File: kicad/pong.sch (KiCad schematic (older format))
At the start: 37 parts, among them J101 power, J102 Y_F, J103 X_F, J104 X, J105 Y, J106 Z, U101 L7805, U102 L7905, U103 TL082, U104 TL082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

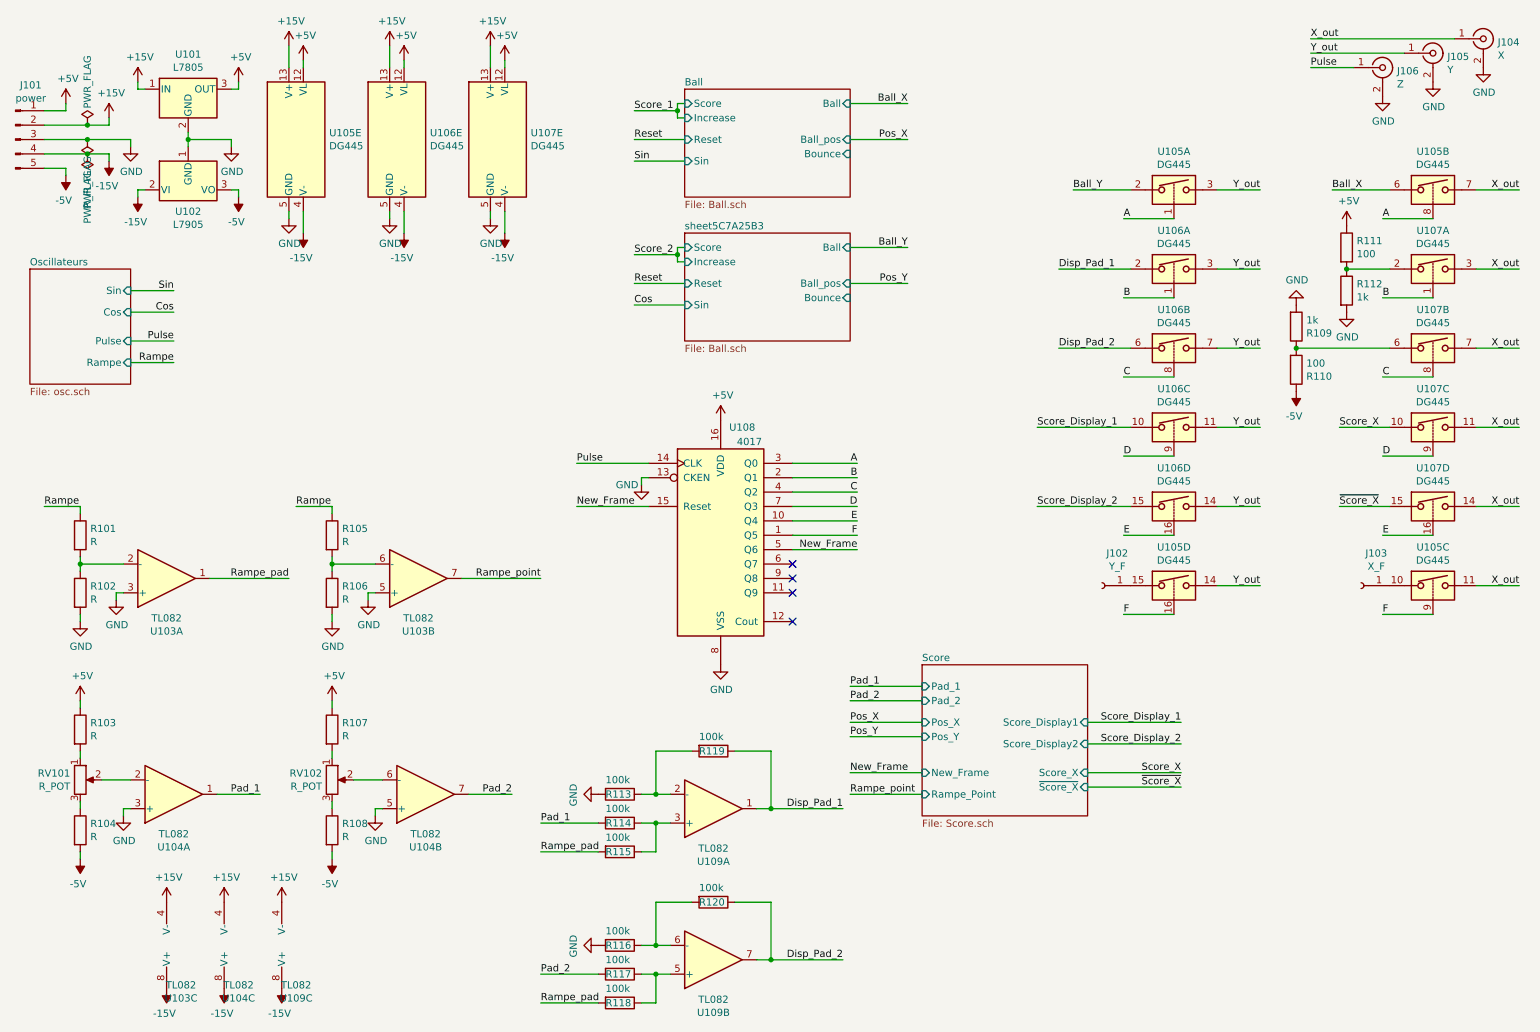
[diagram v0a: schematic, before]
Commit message: Quick fix and documentation
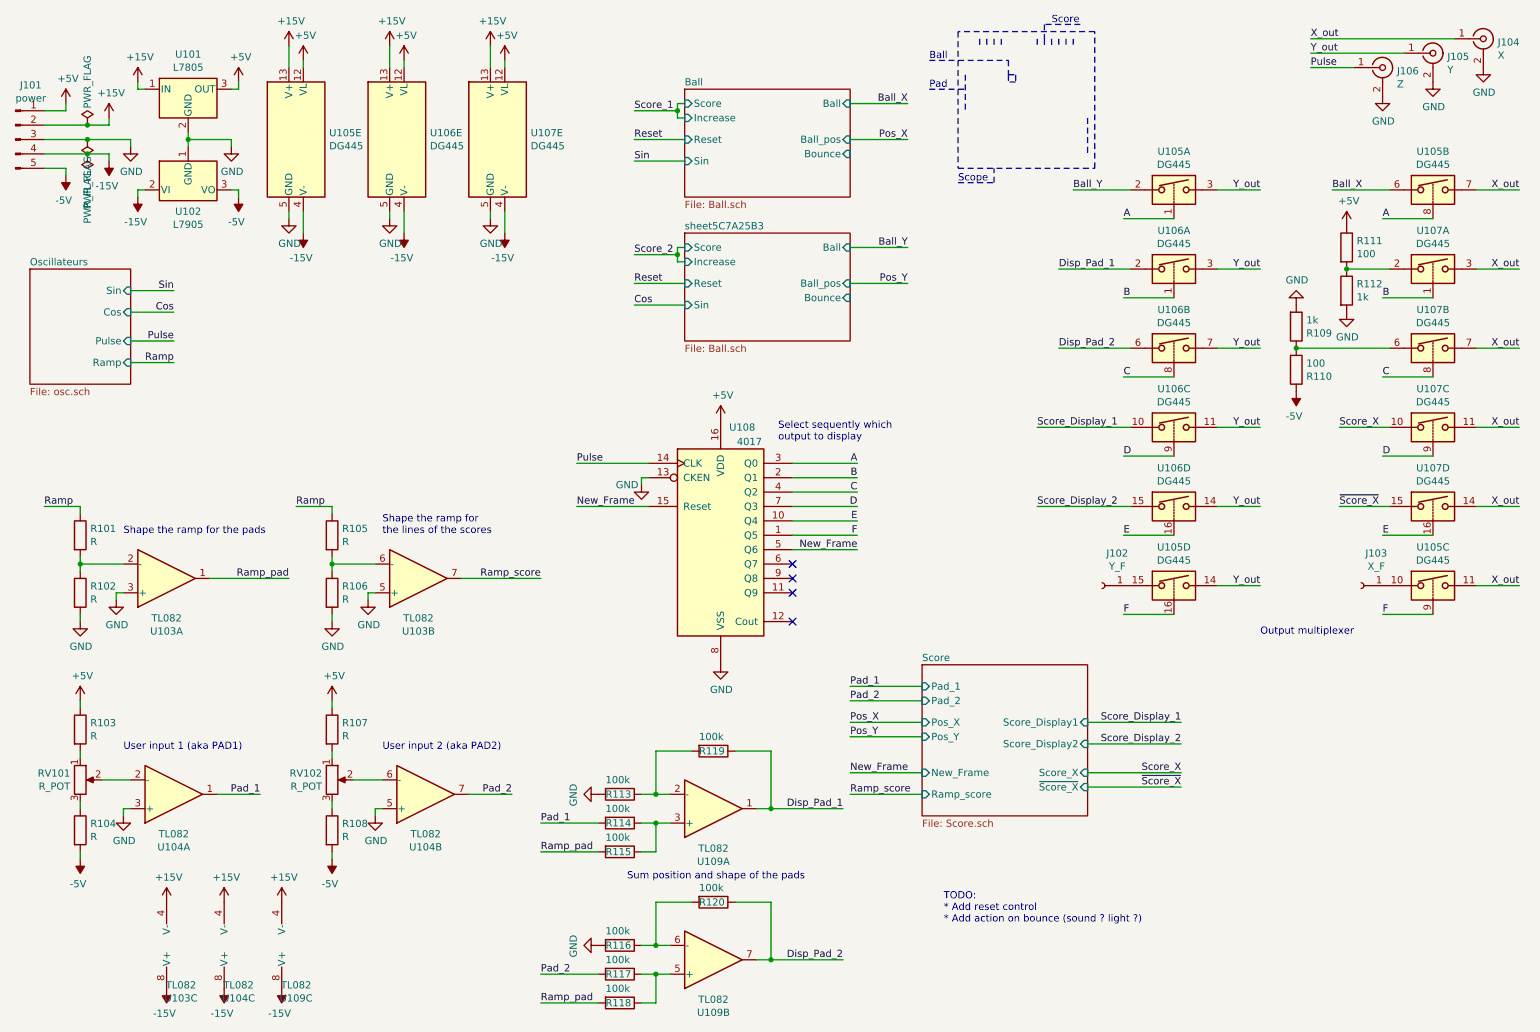
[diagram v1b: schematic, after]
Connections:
- net Rampe renamed Ramp
- net Rampe_pad renamed Ramp_pad
- net Rampe_point renamed Ramp_score
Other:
- note added: "Ball"
- note added: "Output multiplexer"
- note added: "Pad"
- note added: "Scope"
- note added: "Score"
- note added: "Select sequently which\noutput to display"
- note added: "Shape the ramp for \nthe lines of the scores"
- note added: "Shape the ramp for the pads"
- note added: "Sum position and shape of the pads"
- note added: "TODO: \n* Add reset control\n* Add action on bounce (sound ? light ?)"
- note added: "User input 1 (aka PAD1)"
- note added: "User input 2 (aka PAD2)"
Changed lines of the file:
@@
 F2 "Sin" I R 1350 2400 50
 F3 "Cos" I R 1350 2550 50
-F4 "Rampe" I R 1350 2900 50
 F5 "Pulse" I R 1350 2750 50
+F6 "Ramp" I R 1350 2900 50
 $EndSheet
 $Sheet
@@
 F7 "Score_Display2" I R 8000 5550 50
 F8 "Pos_X" I L 6850 5400 50
-F9 "Rampe_Point" I L 6850 5900 50
 F10 "Score_X" I R 8000 5750 50
 F11 "~Score_X" I R 8000 5850 50
+F12 "Ramp_score" I L 6850 5900 50
 $EndSheet
 $Comp
@@
 Pulse
 Text Label 1650 2900 2    50   ~ 0
-Rampe
+Ramp
 Text Label 750  3900 0    50   ~ 0
-Rampe
+Ramp
 Wire Wire Line
 	1900 4400 2450 4400
 Text Label 2450 4400 2    50   ~ 0
-Rampe_pad
+Ramp_pad
 $Comp
 L Device:R R105
@@
 	2750 3900 2500 3900
 Text Label 2500 3900 0    50   ~ 0
-Rampe
+Ramp
 Wire Wire Line
 	3650 4400 4200 4400
 Text Label 4200 4400 2    50   ~ 0
-Rampe_point
+Ramp_score
 $Comp
 L Analog_Switch:DG412xJ U107
@@
 	6350 5900 6850 5900
 Text Label 6350 5900 0    50   ~ 0
-Rampe_point
+Ramp_score
 Wire Wire Line
 	8000 5400 8650 5400
@@
 $EndComp
 Text Label 4200 6300 0    50   ~ 0
-Rampe_pad
+Ramp_pad
 Wire Wire Line
 	5800 6000 6300 6000
@@
 $EndComp
 Text Label 4200 7350 0    50   ~ 0
-Rampe_pad
+Ramp_pad
 Wire Wire Line
 	5800 7050 6300 7050
@@
 	1    0    0    -1
 $EndComp
+Text Notes 7000 6800 0    50   ~ 0
+TODO: \n* Add reset control\n* Add action on bounce (sound ? light ?)
+Text Notes 5850 3450 0    50   ~ 0
+Select sequently which\noutput to display
+Text Notes 9200 4800 0    50   ~ 0
+Output multiplexer
+Text Notes 1300 4100 0    50   ~ 0
+Shape the ramp for the pads
+Text Notes 3100 4100 0    50   ~ 0
+Shape the ramp for \nthe lines of the scores
+Text Notes 1300 5600 0    50   ~ 0
+User input 1 (aka PAD1)
+Text Notes 3100 5600 0    50   ~ 0
+User input 2 (aka PAD2)
+Text Notes 4800 6500 0    50   ~ 0
+Sum position and shape of the pads
+Wire Notes Line width 12 style solid
+	8050 600  7100 600
+Wire Notes Line style solid
+	7150 900  7150 1150
+Wire Notes Line width 12 style solid
+	7100 600  7100 1550
+Wire Notes Line width 12 style solid
+	7100 1550 8050 1550
+Wire Notes Line width 12 style solid
+	8050 1550 8050 600
+Wire Notes Line style solid
+	8000 1200 8000 1450
+Wire Notes Line style solid
+	7250 650  7250 700
+Wire Notes Line style solid
+	7300 650  7300 700
+Wire Notes Line style solid
+	7350 650  7350 700
+Wire Notes Line style solid
+	7400 650  7400 700
+Wire Notes Line style solid
+	7900 650  7900 700
+Wire Notes Line style solid
+	7850 650  7850 700
+Wire Notes Line style solid
+	7800 650  7800 700
+Wire Notes Line style solid
+	7750 650  7750 700
+Wire Notes Line style solid
+	7700 650  7700 700
+Wire Notes Line style solid
+	7650 650  7650 700
+Wire Notes Line style solid
+	7450 900  7450 950
+Wire Notes Line style solid
+	7500 900  7500 950
+Wire Notes Line style solid
+	7450 900  7500 900
+Wire Notes Line style solid
+	7500 950  7450 950
+Text Notes 7100 1650 0    50   ~ 0
+Scope
+Text Notes 6900 1000 0    50   ~ 0
+Pad
+Text Notes 6900 800  0    50   ~ 0
+Ball
+Text Notes 7750 550  0    50   ~ 0
+Score
+Wire Notes Line
+	7450 800  7450 900
+Wire Notes Line
+	6900 800  7450 800
+Wire Notes Line
+	6900 1000 7150 1000
+Wire Notes Line
+	7100 1650 7350 1650
+Wire Notes Line
+	7350 1650 7350 1550
+Wire Notes Line
+	7950 550  7700 550
+Wire Notes Line
+	7700 550  7700 650
 $EndSCHEMATC

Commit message: tests and doc ok
still need some scoring options
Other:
- note added: "TODO: \n* Add reset control\n* Add score control\n* Add action on bounce (sound ? light ?)"
- note removed: "TODO: \n* Add reset control\n* Add action on bounce (sound ? light ?)"
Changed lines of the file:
@@
 S 650  2250 700  800
 U 5C71D21F
-F0 "Oscillateurs" 50
+F0 "Oscillators" 50
 F1 "osc.sch" 50
 F2 "Sin" I R 1350 2400 50
 F3 "Cos" I R 1350 2550 50
-F5 "Pulse" I R 1350 2750 50
-F6 "Ramp" I R 1350 2900 50
+F4 "Pulse" I R 1350 2750 50
+F5 "Ramp" I R 1350 2900 50
 $EndSheet
 $Sheet
 S 5200 1000 1150 750
 U 5C722E04
-F0 "Ball" 50
+F0 "BallX" 50
 F1 "Ball.sch" 50
 F2 "Increase" I L 5200 1200 50
@@
 F7 "Score_Display2" I R 8000 5550 50
 F8 "Pos_X" I L 6850 5400 50
-F10 "Score_X" I R 8000 5750 50
-F11 "~Score_X" I R 8000 5850 50
-F12 "Ramp_score" I L 6850 5900 50
+F9 "Score_X" I R 8000 5750 50
+F10 "~Score_X" I R 8000 5850 50
+F11 "Ramp_score" I L 6850 5900 50
 $EndSheet
 $Comp
@@
 S 5200 2000 1150 750
 U 5C7A25BC
-F0 "sheet5C7A25B3" 50
+F0 "BallY" 50
 F1 "Ball.sch" 50
 F2 "Increase" I L 5200 2200 50
@@
 	1    0    0    -1
 $EndComp
-Text Notes 7000 6800 0    50   ~ 0
-TODO: \n* Add reset control\n* Add action on bounce (sound ? light ?)
+Text Notes 7000 6900 0    50   ~ 0
+TODO: \n* Add reset control\n* Add score control\n* Add action on bounce (sound ? light ?)
 Text Notes 5850 3450 0    50   ~ 0
 Select sequently which\noutput to display
@@
 Sum position and shape of the pads
 Wire Notes Line width 12 style solid
-	8050 600  7100 600
+	10900 5250 9950 5250
 Wire Notes Line style solid
-	7150 900  7150 1150
+	10000 5550 10000 5800
 Wire Notes Line width 12 style solid
-	7100 600  7100 1550
+	9950 5250 9950 6200
 Wire Notes Line width 12 style solid
-	7100 1550 8050 1550
+	9950 6200 10900 6200
 Wire Notes Line width 12 style solid
-	8050 1550 8050 600
+	10900 6200 10900 5250
 Wire Notes Line style solid
-	8000 1200 8000 1450
+	10850 5850 10850 6100
 Wire Notes Line style solid
-	7250 650  7250 700
+	10100 5300 10100 5350
 Wire Notes Line style solid
-	7300 650  7300 700
+	10150 5300 10150 5350
 Wire Notes Line style solid
-	7350 650  7350 700
+	10200 5300 10200 5350
 Wire Notes Line style solid
-	7400 650  7400 700
+	10250 5300 10250 5350
 Wire Notes Line style solid
-	7900 650  7900 700
+	10750 5300 10750 5350
 Wire Notes Line style solid
-	7850 650  7850 700
+	10700 5300 10700 5350
 Wire Notes Line style solid
-	7800 650  7800 700
+	10650 5300 10650 5350
 Wire Notes Line style solid
-	7750 650  7750 700
+	10600 5300 10600 5350
 Wire Notes Line style solid
-	7700 650  7700 700
+	10550 5300 10550 5350
 Wire Notes Line style solid
-	7650 650  7650 700
+	10500 5300 10500 5350
 Wire Notes Line style solid
-	7450 900  7450 950
+	10300 5550 10300 5600
 Wire Notes Line style solid
-	7500 900  7500 950
+	10350 5550 10350 5600
 Wire Notes Line style solid
-	7450 900  7500 900
+	10300 5550 10350 5550
 Wire Notes Line style solid
-	7500 950  7450 950
-Text Notes 7100 1650 0    50   ~ 0
+	10350 5600 10300 5600
+Text Notes 9950 6300 0    50   ~ 0
 Scope
-Text Notes 6900 1000 0    50   ~ 0
+Text Notes 9750 5650 0    50   ~ 0
 Pad
-Text Notes 6900 800  0    50   ~ 0
+Text Notes 9750 5450 0    50   ~ 0
 Ball
-Text Notes 7750 550  0    50   ~ 0
+Text Notes 10600 5200 0    50   ~ 0
 Score
 Wire Notes Line
-	7450 800  7450 900
+	10300 5450 10300 5550
 Wire Notes Line
-	6900 800  7450 800
+	9750 5450 10300 5450
 Wire Notes Line
-	6900 1000 7150 1000
+	9750 5650 10000 5650
 Wire Notes Line
-	7100 1650 7350 1650
+	9950 6300 10200 6300
 Wire Notes Line
-	7350 1650 7350 1550
+	10200 6300 10200 6200
 Wire Notes Line
-	7950 550  7700 550
+	10800 5200 10550 5200
 Wire Notes Line
-	7700 550  7700 650
+	10550 5200 10550 5300
 $EndSCHEMATC
